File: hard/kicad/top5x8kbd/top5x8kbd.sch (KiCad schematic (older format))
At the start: 83 parts, among them J1 IOx, J16 COLUMN, J17 ROW, J2 IOx, J23 MD/VCS1, J33 NES 1, J44 MD/VCS2, J5 TO COMPUTER, J54 NES 2, SW1 1 !, SW10 0 _, SW11 Q ¡, SW12 W ~~, SW13 E é, SW14 R <, SW15 T >, SW16 Y ü, SW17 U ú, SW18 I í, SW19 O ó, SW2 2 @, SW20 P \", SW21 A á, SW22 S ;, SW23 D |, SW24 F [, SW25 G ], SW26 H ^, SW27 J -, SW28 K +, SW29 L =, SW3 3 #, SW30 ENTER ñ, SW31 SHIFT, SW32 Z :, SW33 X ¿, SW34 C ?, SW35 V /, SW36 B *, SW37 N ,, SW38 M ., SW39 ALT, SW4 4 $, SW40 SPACE, SW5 5 %, SW6 6 &, SW7 7 ', SW8 8 (, SW9 9 (, U1 74HC138, U12 74HC174, U13 74HC245, U24 74HC245, U26 74HC174, U34 74HC595, U45 74HC245, U55 74HC595, U9 74HC86

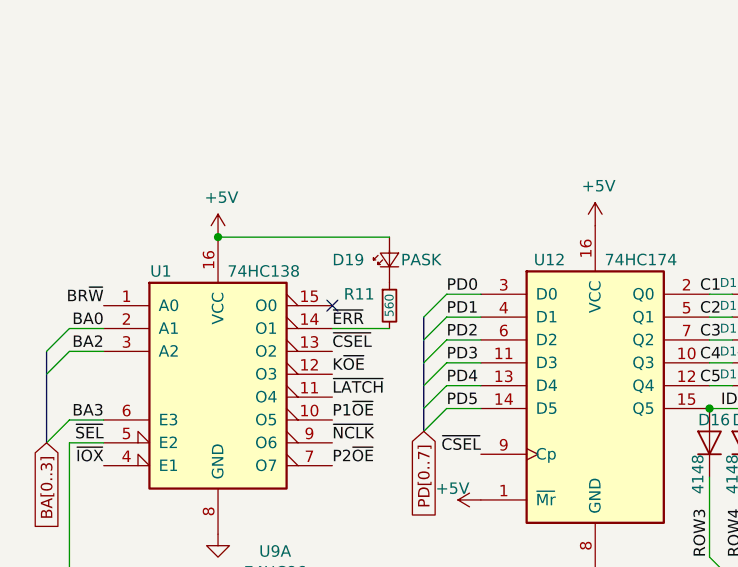
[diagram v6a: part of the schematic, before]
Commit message: back to 7-inch board
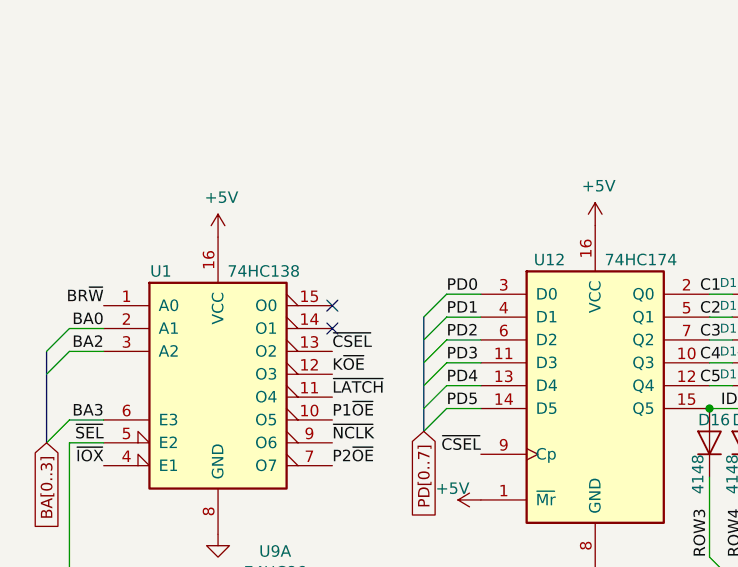
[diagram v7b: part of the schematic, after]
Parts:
- removed D19: PASK, LED_THT:LED_D3.0mm, symbol Device:LED_Small
- removed R11: 560, Resistor_THT:R_Axial_DIN0207_L6.3mm_D2.5mm_P10.16mm_Horizontal, symbol Device:R_Small
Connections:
- net ~ERR: no longer names the net of U1.14 (O1)
- no-connect marks 11 -> 12
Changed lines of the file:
@@
 Text Label 1800 1400 0    50   ~ 0
 K~OE
-Text Label 1800 1200 0    50   ~ 0
-~ERR
 Text Label 800  1100 2    50   ~ 0
 BR~W
@@
 Wire Wire Line
 	8650 5950 8650 6100
-$Comp
-L Device:LED_Small D19
-U 1 1 63960D12
-P 2050 900
-F 0 "D19" V 2050 1150 50  0000 R CNN
-F 1 "PASK" V 2050 850 50  0000 R CNN
-F 2 "LED_THT:LED_D3.0mm" V 2050 900 50  0001 C CNN
-F 3 "~" V 2050 900 50  0001 C CNN
-	1    2050 900
-	0    -1   -1   0
-$EndComp
-$Comp
-L Device:R_Small R11
-U 1 1 639636E2
-P 2050 1100
-F 0 "R11" H 1850 1150 50  0000 L CNN
-F 1 "560" V 2050 1050 39  0000 L CNN
-F 2 "Resistor_THT:R_Axial_DIN0207_L6.3mm_D2.5mm_P10.16mm_Horizontal" H 2050 1100 50  0001 C CNN
-F 3 "~" H 2050 1100 50  0001 C CNN
-	1    2050 1100
-	1    0    0    -1
-$EndComp
-Wire Wire Line
-	1800 1200 2050 1200
-Wire Wire Line
-	2050 800  1300 800
-Connection ~ 1300 800
 $Comp
 L Device:R_Network08 RN22
@@
 	1    0    0    -1
 $EndComp
+NoConn ~ 1800 1200
 Wire Bus Line
 	3550 2300 3850 2300

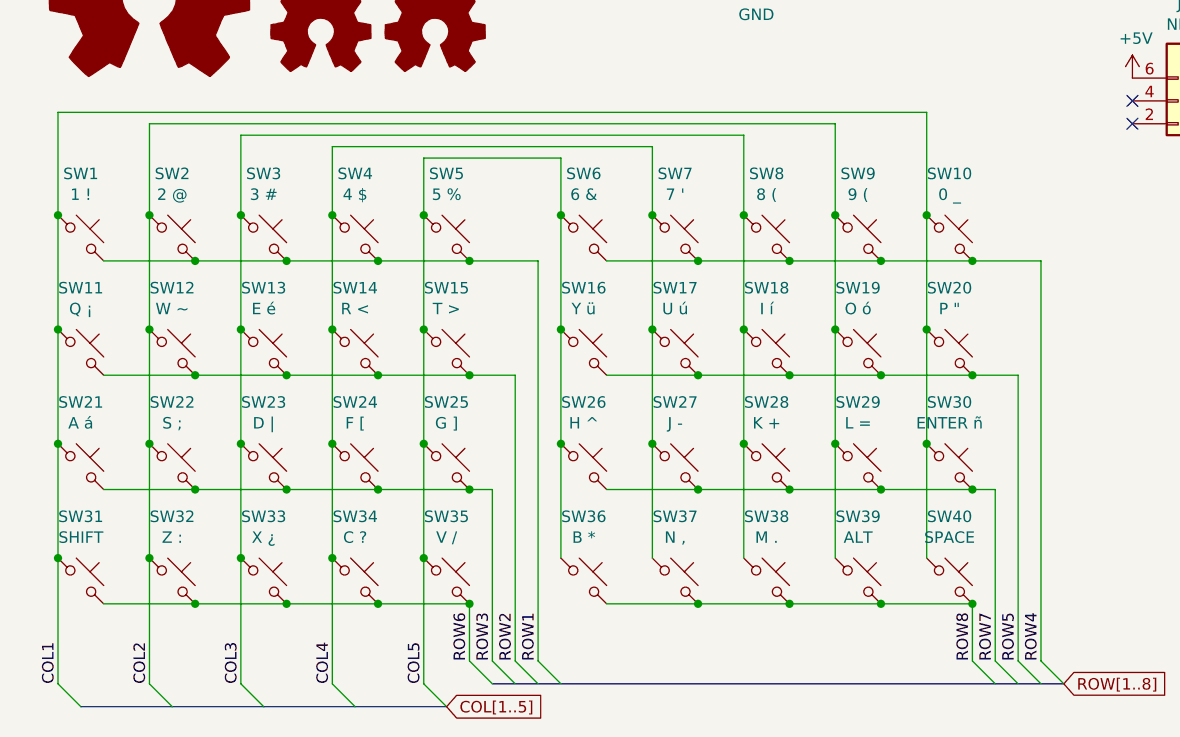
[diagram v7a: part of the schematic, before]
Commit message: flip switches for easier routing
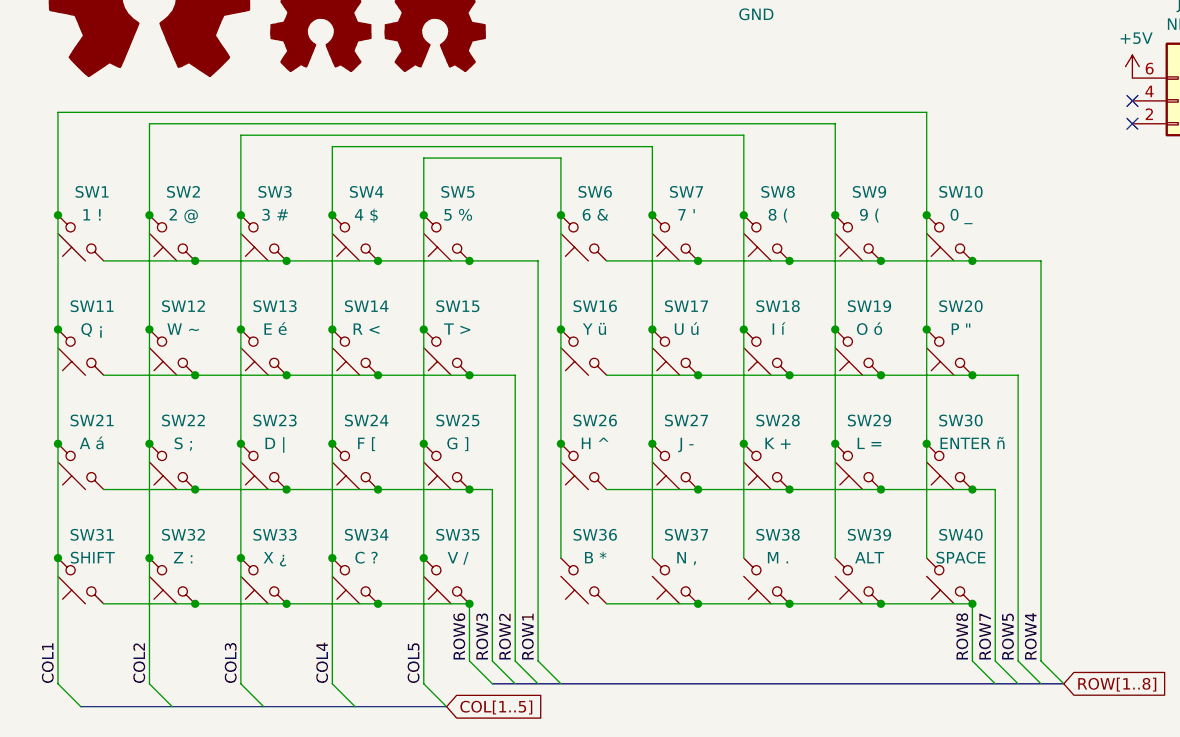
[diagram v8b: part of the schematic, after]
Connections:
- net COL1: now also SW1.2, SW10.2, SW11.2, SW20.2, SW21.2, SW30.2, SW31.2, SW40.2; no longer SW1.1, SW10.1, SW11.1, SW20.1, SW21.1, SW30.1, SW31.1, SW40.1
- net COL2: now also SW12.2, SW19.2, SW2.2, SW22.2, SW29.2, SW32.2, SW39.2, SW9.2; no longer SW12.1, SW19.1, SW2.1, SW22.1, SW29.1, SW32.1, SW39.1, SW9.1
- net COL3: now also SW13.2, SW18.2, SW23.2, SW28.2, SW3.2, SW33.2, SW38.2, SW8.2; no longer SW13.1, SW18.1, SW23.1, SW28.1, SW3.1, SW33.1, SW38.1, SW8.1
- net COL4: now also SW14.2, SW17.2, SW24.2, SW27.2, SW34.2, SW37.2, SW4.2, SW7.2; no longer SW14.1, SW17.1, SW24.1, SW27.1, SW34.1, SW37.1, SW4.1, SW7.1
- net COL5: now also SW15.2, SW16.2, SW25.2, SW26.2, SW35.2, SW36.2, SW5.2, SW6.2; no longer SW15.1, SW16.1, SW25.1, SW26.1, SW35.1, SW36.1, SW5.1, SW6.1
- net ROW1: now also SW1.1, SW2.1, SW3.1, SW4.1, SW5.1; no longer SW1.2, SW2.2, SW3.2, SW4.2, SW5.2
- net ROW2: now also SW11.1, SW12.1, SW13.1, SW14.1, SW15.1; no longer SW11.2, SW12.2, SW13.2, SW14.2, SW15.2
- net ROW3: now also SW21.1, SW22.1, SW23.1, SW24.1, SW25.1; no longer SW21.2, SW22.2, SW23.2, SW24.2, SW25.2
- net ROW4: now also SW10.1, SW6.1, SW7.1, SW8.1, SW9.1; no longer SW10.2, SW6.2, SW7.2, SW8.2, SW9.2
- net ROW5: now also SW16.1, SW17.1, SW18.1, SW19.1, SW20.1; no longer SW16.2, SW17.2, SW18.2, SW19.2, SW20.2
- net ROW6: now also SW31.1, SW32.1, SW33.1, SW34.1, SW35.1; no longer SW31.2, SW32.2, SW33.2, SW34.2, SW35.2
- net ROW7: now also SW26.1, SW27.1, SW28.1, SW29.1, SW30.1; no longer SW26.2, SW27.2, SW28.2, SW29.2, SW30.2
- net ROW8: now also SW36.1, SW37.1, SW38.1, SW39.1, SW40.1; no longer SW36.2, SW37.2, SW38.2, SW39.2, SW40.2
